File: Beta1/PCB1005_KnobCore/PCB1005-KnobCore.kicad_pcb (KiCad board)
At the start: 2 copper layers, 199 x 30.9 mm, 43 parts, among them U1000 MCP3008T-I/SL, U2 MCP3008T-I/SL

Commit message: Rough Placement; pre display
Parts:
- added J1: Axoloti_40Pin, Liberry:Axoloti-40x2_slim, F.Cu at (52.1, -1.27)
- added SPI_CS_0_8: CONN_01X01, Liberry:TH_0.1_1x2_Jumper, F.Cu at (-30.5, -66.0)
- moved REF** 224.1 mm to (-27.5, -19.0)
- moved REF** 221.0 mm to (-24.9, -34.2)
- moved REF** 74.4 mm to (-17.3, -72.3)
- moved U2 69.6 mm to (0.00, -61.0)
- moved +3.3V1 68.6 mm to (-60.5, -28.5)
- moved A0 68.6 mm to (-60.6, -31.0)
- moved A0 68.6 mm to (-58.0, -31.0)
- moved A1 68.6 mm to (-60.5, -10.7)
- moved A1 68.6 mm to (-58.0, -10.7)
- moved A2 68.6 mm to (-60.5, -8.17)
- moved A2 68.6 mm to (-58.0, -8.17)
- moved A3 68.6 mm to (-60.5, -5.63)
- moved A3 68.6 mm to (-58.0, -5.63)
- moved GND1000 68.6 mm to (-60.5, -13.2)
- moved MISO1 68.6 mm to (-60.5, -18.3)
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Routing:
- net +3V3: track 406.8 -> 0.00 mm, vias 2 -> 0
- net GND: track 384.2 -> 0.00 mm, vias 1 -> 0
- net /P7: track 129.8 -> 0.00 mm
- net /P15: track 127.4 -> 0.00 mm
- net /P6: track 108.7 -> 0.00 mm
- net /P14: track 107.6 -> 0.00 mm
- net /P13: track 90.1 -> 0.00 mm
- net /P5: track 89.2 -> 0.00 mm
- net /MOSI: track 81.3 -> 0.00 mm, vias 2 -> 0
- net /MISO: track 78.3 -> 0.00 mm, vias 2 -> 0
- net /P4: track 69.5 -> 0.00 mm
- net /P12: track 69.0 -> 0.00 mm
- net /CS_LED_8_15: track 61.4 -> 0.00 mm
- net /SPICLK: track 60.7 -> 0.00 mm
- net /P11: track 48.4 -> 0.00 mm
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- removed copper zone on F.Cu, net GND
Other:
- board size 199 x 30.9 mm -> 160 x 50 mm

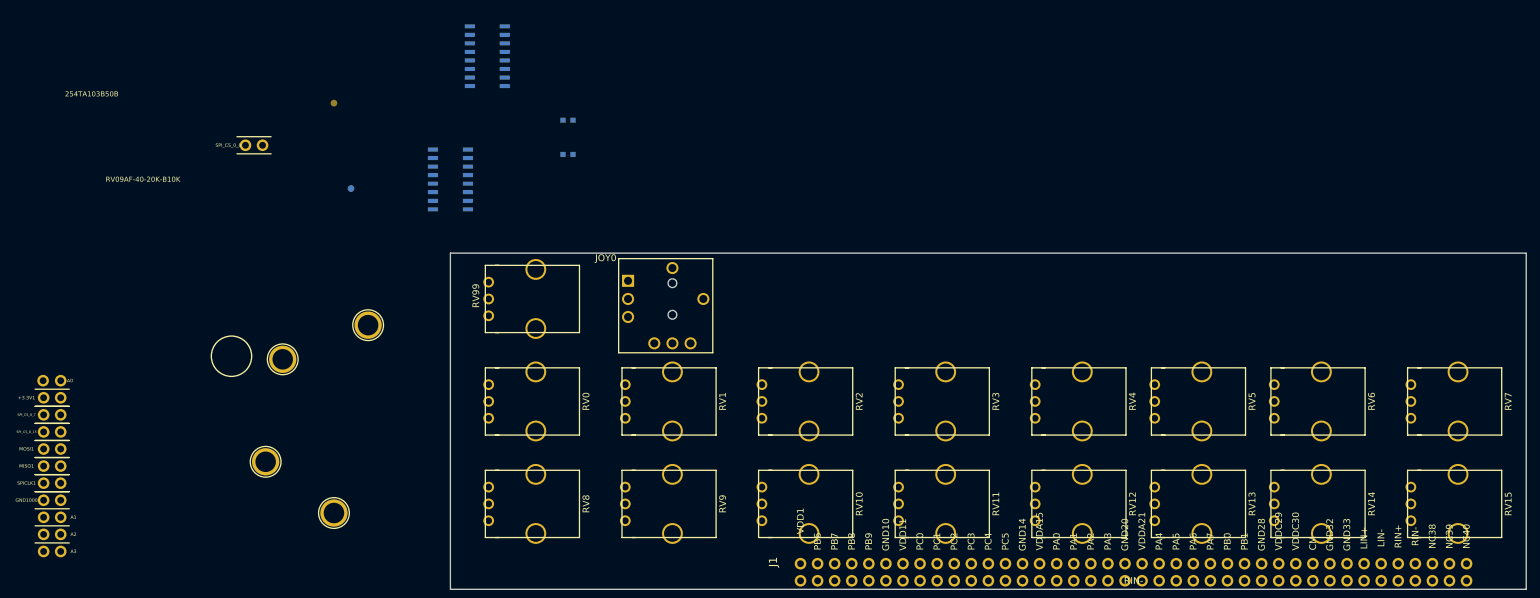
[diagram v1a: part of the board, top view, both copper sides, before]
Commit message: Added OLED to SCH. PCB needs update.
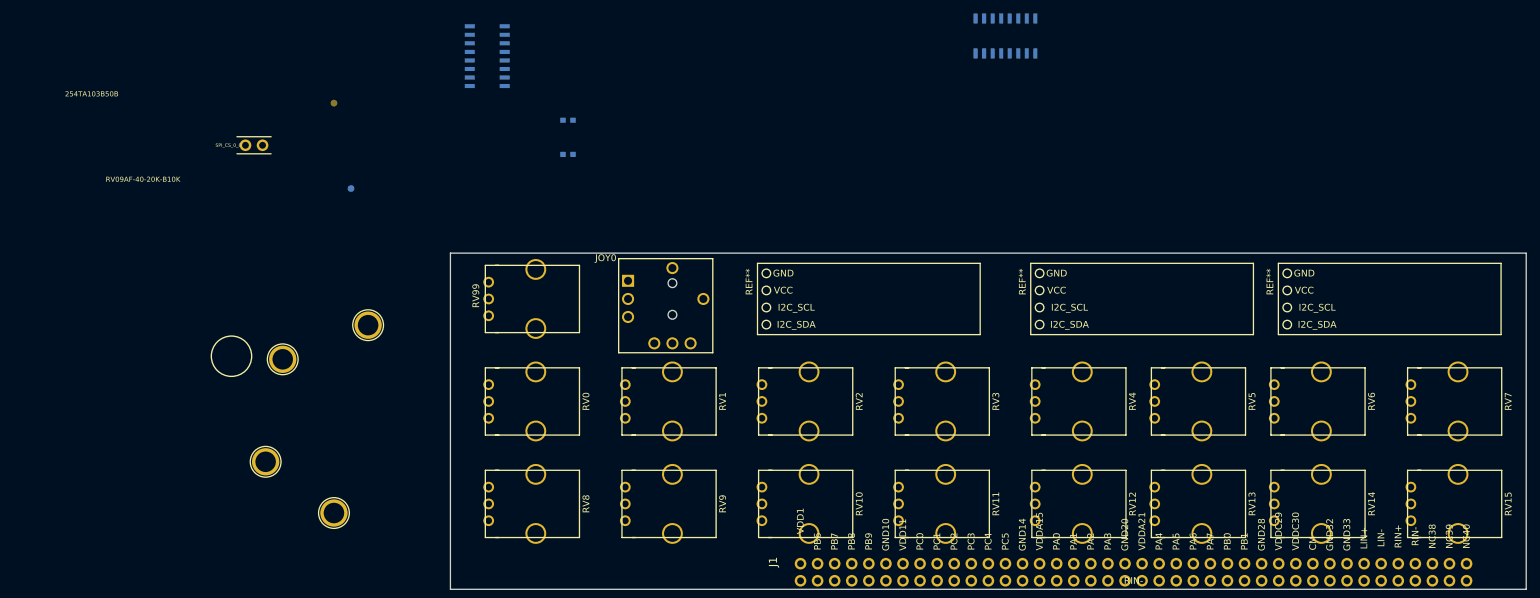
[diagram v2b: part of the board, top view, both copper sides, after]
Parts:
- removed +3.3V1, GND1000, MISO1, MOSI1, SPICLK1, SPI_CS_0_7, SPI_CS_8_15: CONN_01X01, Liberry:TH_0.1_1x2_Jumper
- removed A0 (x2), A1 (x2), A2 (x2), A3 (x2): CONN_01X01, Liberry:single_0.1
- added REF**: 128x32_Footprint_guess, Liberry:128x32_Footprint_guess, F.Cu at (139.7, -43.2)
- added REF**: 128x32_Footprint_guess, Liberry:128x32_Footprint_guess, F.Cu at (102.9, -43.2)
- added REF**: 128x32_Footprint_guess, Liberry:128x32_Footprint_guess, F.Cu at (62.2, -43.2)
- moved U2 85.3 mm to (82.5, -82.3), turned to 0 degrees
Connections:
- net /ANALOG_OUT renamed Net-(J1-Pad22)
- net /KB_A0 renamed Net-(J1-Pad10)
- net /KB_A1 renamed Net-(J1-Pad11)
- net /KB_A2 renamed Net-(J1-Pad12)
- net /KB_A3 renamed Net-(J1-Pad16)
- net /KB_A4 renamed Net-(J1-Pad18)
- net /KB_A5 renamed Net-(J1-Pad19)
- net /KB_IRQ renamed Net-(J1-Pad27)
- net /SPI_CS_LED0 renamed Net-(J1-Pad13)
- J1 pad 1: /VCC_A -> /+3.3V
- J1 pad 15: /VCC_B -> /+3.3V
- J1 pad 2: /KNOB_CS_8_15 -> /CS_8_15
- J1 pad 21: /VCC_B -> /+3.3V
- J1 pad 29: /VCC_C -> /+3.3V
- J1 pad 3: /KNOB_CS_0_7 -> /CS_0_7
- J1 pad 30: /VCC_C -> /+3.3V
- J1 pad 7: /VCC_A -> /+3.3V
- J1 pad 8: /JOY_Y -> /JOY_0
- J1 pad 9: /JOY_X -> /JOY_1
- JOY0 pad R1.2: Net-(A1-Pad1) -> /JOY_0
- JOY0 pad R2.2: Net-(A2-Pad1) -> /JOY_1
- JOY0 pad S1.2: Net-(A3-Pad1) -> /JOY_SW
- U1000 pad 10: /CS_R0_7 -> /CS_0_7
- U1000 pad 11: /MOSI -> /SPI_MOSI
- U1000 pad 12: /MISO -> /SPI_MISO
- U1000 pad 13: /SPICLK -> /SPI_CLK
- U2 pad 10: /CS_LED_8_15 -> /CS_8_15
- U2 pad 11: /MOSI -> /SPI_MOSI
- U2 pad 12: /MISO -> /SPI_MISO
- U2 pad 13: /SPICLK -> /SPI_CLK

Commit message: PCB Placed, ready to route.
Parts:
- removed the REF** at (139.7, -43.2)
- removed the REF** at (102.9, -43.2)
- removed the REF** at (-12.2, -39.3)
- removed the REF** at (62.2, -43.2)
- removed SPI_CS_0_8: CONN_01X01, Liberry:TH_0.1_1x2_Jumper
- added C1: 0.1u, Capacitors_SMD:C_0603, F.Cu at (147.3, -48.9)
- added RC0: 10K, Resistors_SMD:R_0603, F.Cu at (147.3, -45.1)
- added RC10: 10K, Resistors_SMD:R_0603, F.Cu at (135.3, -43.2)
- added RC20: 10K, Resistors_SMD:R_0603, F.Cu at (135.3, -39.4)
- added RC30: 10K, Resistors_SMD:R_0603, F.Cu at (147.3, -39.4)
- added RC40: 10K, Resistors_SMD:R_0603, F.Cu at (147.3, -43.2)
- added RD0: 10K, Resistors_SMD:R_0603, F.Cu at (147.3, -47.0)
- added RD10: 10K, Resistors_SMD:R_0603, F.Cu at (135.3, -45.1)
- added RD20: 10K, Resistors_SMD:R_0603, F.Cu at (135.3, -41.3)
- added RD30: 10K, Resistors_SMD:R_0603, F.Cu at (147.3, -37.5)
- added RD40: 10K, Resistors_SMD:R_0603, F.Cu at (147.3, -41.3)
- added REF**: Fiducial_1mm_Dia_2.54mm_Outer_CopperBottom, Fiducials:Fiducial_1mm_Dia_2.54mm_Outer_CopperBottom, B.Cu at (157.5, -48.3)
- added REF**: 1pin, Connect:1pin, F.Cu at (156.5, -40.0)
- added REF**: 1pin, Connect:1pin, F.Cu at (156.5, -10.0)
- added RR0: 10K, Resistors_SMD:R_0603, F.Cu at (135.3, -47.0)
- added U10: OLED_128x32_I2C, Liberry:OLED_128x32, F.Cu at (47.0, -47.2)
- added U20: OLED_128x32_I2C, Liberry:OLED_128x32, F.Cu at (87.7, -47.2)
- added U30: OLED_128x32_I2C, Liberry:OLED_128x32, F.Cu at (124.5, -47.2)
- added U5: I2C_1x4MUX_TCA9546A, Liberry:SOIC-16_1.27x5.4, F.Cu at (141.1, -43.8)
- C1000, C2, U1000, U2: moved to F.Cu
- REF**: moved to B.Cu
- moved REF** 181.5 mm to (157.5, -2.54)
- moved C2 90.5 mm to (105.4, -48.3), turned to 0 degrees
- moved RV4 85.2 mm to (10.2, -12.7), turned to 90 degrees
- moved REF** 84.2 mm to (54.0, -40.0)
- moved RV5 82.7 mm to (30.5, -12.7)
- moved RV10 80.2 mm to (132.1, -27.9)
- moved RV11 80.2 mm to (152.4, -27.9)
- moved RV7 80.2 mm to (71.1, -12.7)
- moved RV9 80.2 mm to (111.8, -27.9)
- moved RV6 80.2 mm to (50.8, -12.7)
- moved RV8 80.2 mm to (91.4, -27.9)
- moved REF** 77.0 mm to (55.9, -48.3)
- moved U1000 72.7 mm to (68.6, -43.2), turned to 0 degrees
- moved C1000 50.1 mm to (64.8, -48.3), turned to 0 degrees
- moved U2 47.3 mm to (109.2, -43.2)
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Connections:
- J1 pad 1: /+3.3V -> +3V3
- J1 pad 10: Net-(J1-Pad10) -> /!OLED_RESET
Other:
- board text added: "PCB1005_KnobCore_2017-05-18 16CH Knobs + Vol + JoyXY + OLED https://github.com/Believotron/BelievotronWanderlustHardware"
- board text added: "TCA9546A"
- board text added: "You are more beautiful than you will ever know"
- board text removed: "(Bottom Row) SPI_CS_8_15"
- board text removed: "(Data In) MOSI"
- board text removed: "(Data Out) MISO"
- board text removed: "(Joy Button) A3"
- board text removed: "(Joy X) A2"
- board text removed: "(Joy Y) A1"
- board text removed: "(Top Row) SPI_CS_0_7"
- board text removed: "(Volume) A0"
- board text removed: "+3.3V"
- board text removed: "0.1 uF"
- board text removed: "GND"
- board text removed: "NO: Req ext / micro pullup Button push connects to GND."
- board text removed: "PCB1000_KNOBS16_2017-03-31 Believotron 16CH Analog Pot to SPI. Beta-1 https://github.com/Believotron/BelievotronWanderlustHardware"
- board text removed: "SPICLK"
- board text removed: "You are more beautiful than you will ever know."

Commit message: Ready for fab
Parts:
- moved C1000 4.96 mm to (61.0, -45.1), turned to 270 degrees
- moved C2 3.70 mm to (102.2, -46.4), turned to 270 degrees
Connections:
- net /I2C_SC3 renamed /I2C_SCL3
- net /I2C_SD3 renamed /I2C_SDA3
- J1 pad 15: /+3.3V -> +3V3
- J1 pad 21: /+3.3V -> +3V3
- J1 pad 29: /+3.3V -> +3V3
- J1 pad 30: /+3.3V -> +3V3
- J1 pad 7: /+3.3V -> +3V3
- RC10 pad 2: /I2C_SC0 -> /I2C_SCL0
- RC20 pad 2: /I2C_SC1 -> /I2C_SCL1
- RC30 pad 2: /I2C_SC2 -> /I2C_SCL2
- RD10 pad 2: /I2C_SD0 -> /I2C_SDA0
- RD20 pad 2: /I2C_SD1 -> /I2C_SDA1
- RD30 pad 2: /I2C_SD2 -> /I2C_SDA2
- U10 pad 2: /+3.3V -> +3V3
- U20 pad 2: /+3.3V -> +3V3
- U30 pad 2: /+3.3V -> +3V3
- U5 pad 10: /I2C_SC2 -> /I2C_SCL2
- U5 pad 4: /I2C_SD0 -> /I2C_SDA0
- U5 pad 5: /I2C_SC0 -> /I2C_SCL0
- U5 pad 6: /I2C_SD1 -> /I2C_SDA1
- U5 pad 7: /I2C_SC1 -> /I2C_SCL1
- U5 pad 9: /I2C_SD2 -> /I2C_SDA2
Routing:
- net +3V3: track 0.00 -> 609.1 mm, vias 0 -> 8
- net GND: track 0.00 -> 284.5 mm, vias 0 -> 7
- net /VOLUME: track 0.00 -> 203.4 mm, vias 0 -> 1
- net /JOY_SW: track 0.00 -> 195.1 mm, vias 0 -> 2
- net /JOY_1: track 0.00 -> 132.7 mm, vias 0 -> 1
- net /SPI_CLK: track 0.00 -> 132.0 mm, vias 0 -> 5
- net /I2C_SCL: track 0.00 -> 128.8 mm
- net /I2C_SDA: track 0.00 -> 128.4 mm, vias 0 -> 2
- net /JOY_0: track 0.00 -> 126.8 mm, vias 0 -> 1
- net /SPI_MOSI: track 0.00 -> 124.6 mm, vias 0 -> 4
- net /SPI_MISO: track 0.00 -> 124.1 mm, vias 0 -> 5
- net /P12: track 0.00 -> 116.9 mm
- net /!OLED_RESET: track 0.00 -> 116.0 mm, vias 0 -> 2
- net /I2C_SDA0: track 0.00 -> 106.9 mm, vias 0 -> 4
- net /I2C_SCL0: track 0.00 -> 105.6 mm, vias 0 -> 4
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- added copper zone on B.Cu, net GND
- added copper zone on F.Cu, net GND

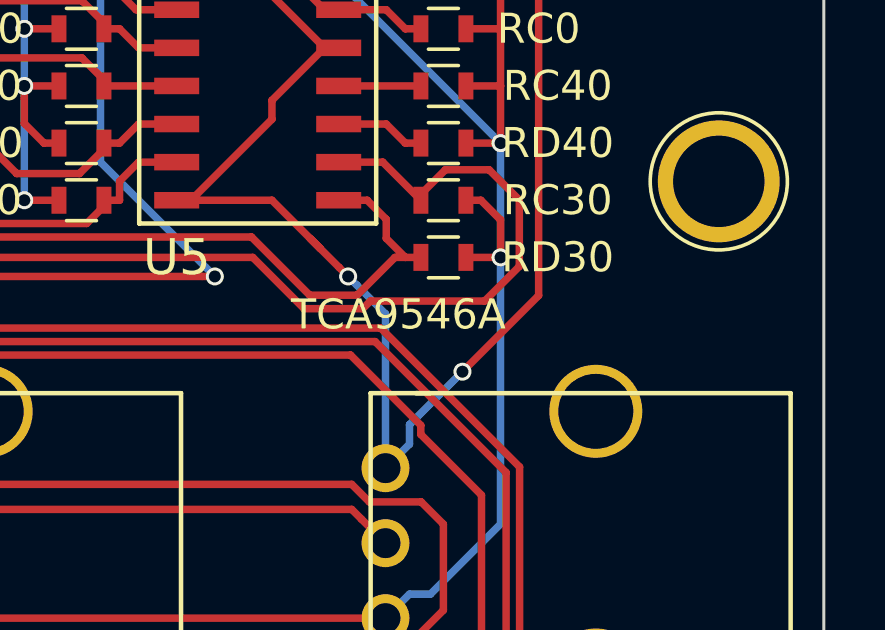
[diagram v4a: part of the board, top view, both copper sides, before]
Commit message: Updated MPN to TCA9546ADR
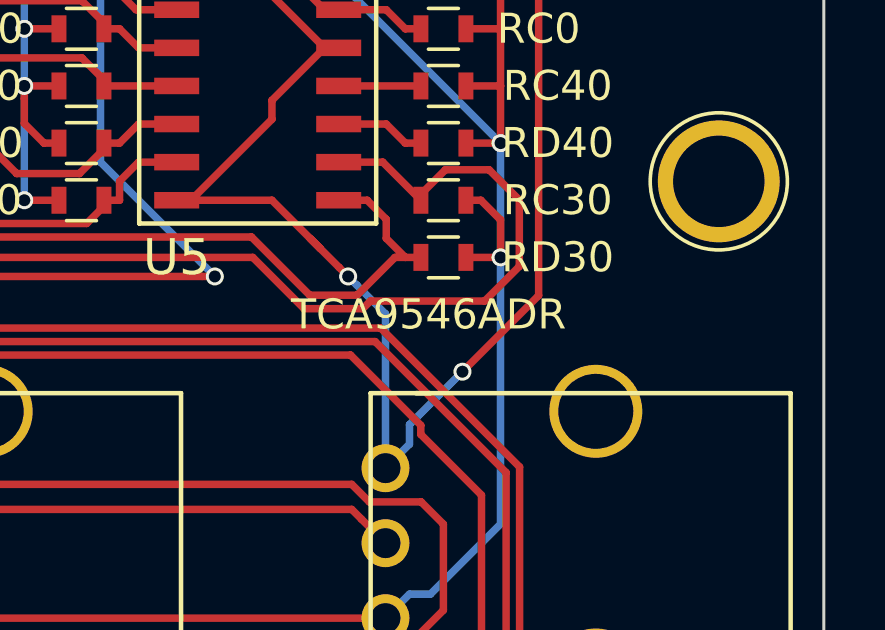
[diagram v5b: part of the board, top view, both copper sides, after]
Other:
- board text added: "TCA9546ADR"
- board text removed: "TCA9546A"
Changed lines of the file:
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@@
   (general
     (links 333)
-    (no_connects 1)
-    (area -0.050001 -50.050001 160.050001 0.050001)
+    (no_connects 0)
+    (area -0.635 -54.272143 185.860001 0.335)
     (thickness 1.6)
     (drawings 24)
@@
     (effects (font (size 1 1) (thickness 0.15)))
   )
-  (gr_text TCA9546A (at 142.24 -35.56) (layer F.SilkS)
+  (gr_text TCA9546ADR (at 142.24 -35.56) (layer F.SilkS)
     (effects (font (size 1 1) (thickness 0.15)) (justify left))
   )

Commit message: Initial Placement
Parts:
- removed RV10, RV11, RV12, RV13, RV14, RV15, RV8, RV9, RV99: POT, Liberry:RV09AF-40-20K-B10K
- added JOY1: XYJOY, Liberry:XY_JOY_254TA103B50B, F.Cu at (71.1, -15.2)
- added JOY2: XYJOY, Liberry:XY_JOY_254TA103B50B, F.Cu at (106.7, -15.2)
- added JOY3: XYJOY, Liberry:XY_JOY_254TA103B50B, F.Cu at (142.2, -15.2)
- added RV_VOL1: POT, Liberry:RV09AF-40-20K-B10K, F.Cu at (17.8, -15.2)
- moved RD10 121.5 mm to (14.0, -38.1), turned to 180 degrees
- moved RC10 121.3 mm to (14.0, -40.6), turned to 180 degrees
- moved RV6 93.2 mm to (142.2, -30.5)
- moved RV4 80.7 mm to (88.9, -30.5), turned to 270 degrees
- moved RV5 78.2 mm to (106.7, -30.5)
- moved RD20 70.6 mm to (64.8, -38.1), turned to 180 degrees
- moved RC20 70.5 mm to (64.8, -40.6), turned to 180 degrees
- moved RV7 56.2 mm to (124.5, -30.5)
- moved REF** 53.4 mm to (2.54, -45.7)
- moved U10 36.9 mm to (10.2, -45.9)
- moved C1000 33.7 mm to (44.5, -15.8)
- moved RD0 33.0 mm to (115.6, -38.1)
- moved C2 32.1 mm to (116.8, -17.8)
- moved RC0 32.1 mm to (115.6, -40.6)
- moved U1000 31.8 mm to (53.3, -15.2)
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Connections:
- net Net-(J1-Pad27) renamed /JOY_3_SW
- J1 pad 26: /JOY_SW -> /JOY_2_SW
- J1 pad 8: /JOY_0 -> /JOY_0_SW
- J1 pad 9: /JOY_1 -> /JOY_1_SW
- U2 pad 1: /P8 -> /JOY_0_0
- U2 pad 2: /P9 -> /JOY_0_1
- U2 pad 3: /P10 -> /JOY_1_0
- U2 pad 4: /P11 -> /JOY_1_1
- U2 pad 5: /P12 -> /JOY_2_0
- U2 pad 6: /P13 -> /JOY_2_1
- U2 pad 7: /P14 -> /JOY_3_0
- U2 pad 8: /P15 -> /JOY_3_1
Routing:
- net +3V3: track 609.1 -> 0.00 mm, vias 8 -> 0
- net GND: track 284.5 -> 0.00 mm, vias 7 -> 0
- net /VOLUME: track 203.4 -> 0.00 mm, vias 1 -> 0
- net /JOY_SW: track 195.1 -> 0.00 mm, vias 2 -> 0
- net /JOY_1: track 132.7 -> 0.00 mm, vias 1 -> 0
- net /SPI_CLK: track 132.0 -> 0.00 mm, vias 5 -> 0
- net /I2C_SCL: track 128.8 -> 0.00 mm
- net /I2C_SDA: track 128.4 -> 0.00 mm, vias 2 -> 0
- net /JOY_0: track 126.8 -> 0.00 mm, vias 1 -> 0
- net /SPI_MOSI: track 124.6 -> 0.00 mm, vias 4 -> 0
- net /SPI_MISO: track 124.1 -> 0.00 mm, vias 5 -> 0
- net /P12: track 116.9 -> 0.00 mm
- net /!OLED_RESET: track 116.0 -> 0.00 mm, vias 2 -> 0
- net /I2C_SDA0: track 106.9 -> 0.00 mm, vias 4 -> 0
- net /I2C_SCL0: track 105.6 -> 0.00 mm, vias 4 -> 0
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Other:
- board size 160 x 50 mm -> 160 x 46 mm
- board text added: "PCB1005_KnobCore_2017-05-31 16CH Knobs + Vol + JoyXY + OLED https://github.com/Believotron/BelievotronWanderlustHardware"
- board text removed: "PCB1005_KnobCore_2017-05-18 16CH Knobs + Vol + JoyXY + OLED https://github.com/Believotron/BelievotronWanderlustHardware"

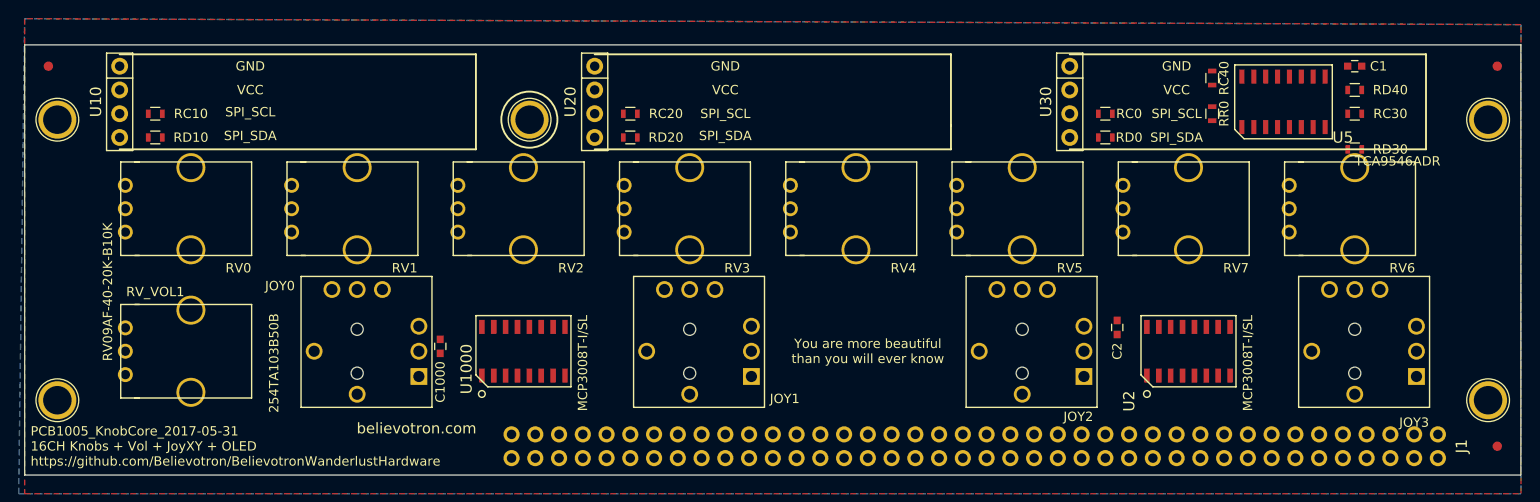
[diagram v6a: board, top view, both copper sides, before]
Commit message: Added CYA TH for I2C3. Cleaned up Silkscreen.
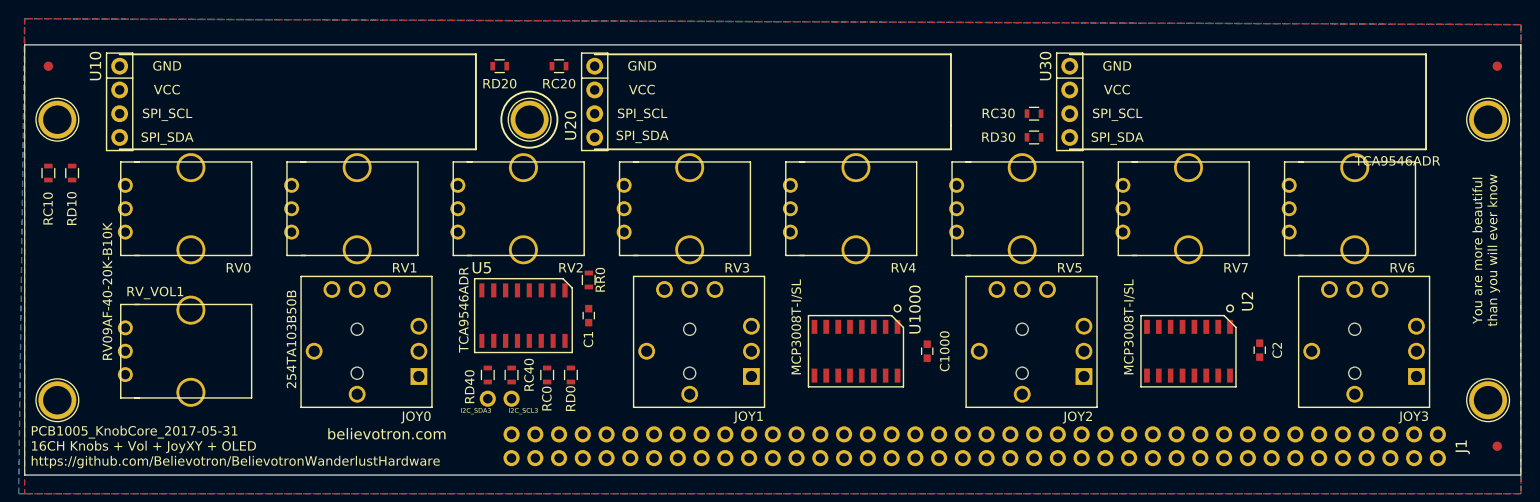
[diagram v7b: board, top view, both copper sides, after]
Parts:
- added I2C_SCL3: CONN_01X01, Liberry:single_0.1, F.Cu at (52.1, -10.2)
- added I2C_SDA3: CONN_01X01, Liberry:single_0.1, F.Cu at (49.5, -10.2)
- moved RD40 97.6 mm to (49.5, -12.7), turned to 270 degrees
- moved C1 86.1 mm to (60.3, -19.1), turned to 90 degrees
- moved U5 84.4 mm to (53.3, -19.1), turned to 180 degrees
- moved RC40 81.4 mm to (52.1, -12.7)
- moved RR0 69.0 mm to (60.3, -22.9)
- moved RC0 65.9 mm to (55.9, -12.7), turned to 90 degrees
- moved RD0 62.5 mm to (58.4, -12.7), turned to 90 degrees
- moved C1000 52.1 mm to (96.5, -15.2), turned to 90 degrees
- moved U1000 35.6 mm to (88.9, -15.2), turned to 180 degrees
- moved RD30 34.3 mm to (108.0, -38.1), turned to 0 degrees
- moved RC30 34.3 mm to (108.0, -40.6), turned to 0 degrees
- moved RD20 15.9 mm to (50.8, -45.7)
- moved C2 15.4 mm to (132.1, -15.4)
- moved RC10 13.1 mm to (2.54, -34.3), turned to 90 degrees
- moved RD10 9.67 mm to (5.08, -34.3), turned to 90 degrees
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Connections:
- JOY0 pad R1.2: /JOY_0 -> /JOY_0_0
- JOY0 pad R2.2: /JOY_1 -> /JOY_0_1
- JOY0 pad S1.2: /JOY_SW -> /JOY_0_SW
